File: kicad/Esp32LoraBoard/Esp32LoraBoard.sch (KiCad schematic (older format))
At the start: 13 parts, among them J1 USB_B_Micro, J2 Power-Selector, J3 Testpoints, U1 LM3940IMP-3.3, U2 ESP32-WROOM-32, U3 RFM95W-868S2

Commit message: Diagram approved
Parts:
- added C5, C6: 1n, Capacitor_SMD:C_1206_3216Metric_Pad1.42x1.75mm_HandSolder, symbol Device:C_Small
- added J4: ESP_PROG_JTAG, symbol Connector_Generic:Conn_02x05_Odd_Even
- added J5: Prog, symbol Connector:Conn_01x05_Male
- added Q1: UMH3N, SOT65P230X110-6N, symbol UMH3N:UMH3N
- added R2: 10k, Resistor_SMD:R_1206_3216Metric_Pad1.42x1.75mm_HandSolder, symbol Device:R
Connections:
- net +3V3: now also R2.1
- net GND: now also C5.2, C6.1, J4.3 (Pin_3), J4.5 (Pin_5), J4.7 (Pin_7), J4.9 (Pin_9), J5.1 (Pin_1)
- net TMS: now reaches U2.13 (IO14)
- net TMS: now also J4.2 (Pin_2)
- net TDI: now reaches U2.14 (IO12)
- net TDI: now also J4.8 (Pin_8)
- net TCK: now reaches U2.16 (IO13)
- net TCK: now also J4.4 (Pin_4)
- net TDO: now reaches U2.23 (IO15)
- net TDO: now also J4.6 (Pin_6)
- net Boot: now reaches U2.25 (IO0)
- net Boot: now also C6.2, Q1.3 (C2), R2.2
- net Reset: now reaches R1.2, U2.3 (EN)
- net Reset: now also C5.1, Q1.6 (C1)
- net RX: now reaches U2.34 (RXD0/IO3)
- net RX: now also J5.4 (Pin_4)
- net TX: now reaches U2.35 (TXD0/IO1)
- net TX: now also J5.3 (Pin_3)
- new net DTR: J5.5 (Pin_5), Q1.1 (E1), Q1.5 (B2)
- new net RTS: J5.2 (Pin_2), Q1.2 (B1), Q1.4 (E2)
- no-connect marks 31 -> 26
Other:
- note added: "Boot"
- note added: "GND"
- note added: "RTS"
- note added: "RX"
- note added: "TX"
- moved on the sheet: R1

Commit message: .
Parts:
- removed J3: Testpoints, Connector_PinHeader_2.54mm:PinHeader_1x03_P2.54mm_Vertical, symbol Connector:Conn_01x03_Male
- added J3: Testpoints, symbol Connector:Conn_01x04_Male
- added J6: ext_Measure, symbol Connector:Screw_Terminal_01x04
- added J7: Measurement-Selector, Connector_PinHeader_2.54mm:PinHeader_1x03_P2.54mm_Vertical, symbol Connector:Conn_01x03_Male
- added Q2: Q_NMOS_GSD, symbol Device:Q_NMOS_GSD
- added Q3: SI2301DS, symbol Device:Q_PMOS_GSD
- added R3, R4: 10k, Resistor_SMD:R_1206_3216Metric_Pad1.42x1.75mm_HandSolder, symbol Device:R
- added R5, R6: optional, Resistor_SMD:R_1206_3216Metric_Pad1.42x1.75mm_HandSolder, symbol Device:R
- added R7, R8: 100k, symbol Device:R
- added TP1: TestPoint, symbol Connector:TestPoint
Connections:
- net +3V3: now also C2.1, J2.3 (Pin_3), U1.3 (OUT), J3.4 (Pin_4); no longer C3.1, C4.1, J2.2 (Pin_2), R1.1, R2.1, U2.2 (VDD), U3.13 (3.3V)
- net GND: now also J3.1 (Pin_1), Q2.2 (S), R4.2, R7.2
- net UBAT_ENABLE: now reaches U2.10 (IO25)
- net UBAT_ENABLE: now also Q3.1 (G), R8.2
- net U_EXT_ENABLE: now reaches U2.26 (IO4)
- net U_EXT_ENABLE: now also Q2.1 (G), R7.1
- net UBAT_MEASURE: now reaches U2.6 (IO34)
- net UBAT_MEASURE: now also R3.2, R4.1, TP1.1
- net U_EXT_MEASURE: now reaches U2.7 (IO35)
- net U_EXT_MEASURE: now also J6.2 (Pin_2), R5.2, R6.1
- net V-Batt: now reaches BT1.1 (+), J2.1 (Pin_1)
- net V-Batt: now also J3.2 (Pin_2)
- new net: Q3.2 (S), R3.1
- new net: J6.1 (Pin_1), Q2.3 (D), R6.2
- new net: J6.3 (Pin_3), J7.2 (Pin_2), R5.1
- new net: J6.4 (Pin_4), J7.1 (Pin_1)
- new net VCC: C3.1, C4.1, J2.2 (Pin_2), J3.3 (Pin_3), J7.3 (Pin_3), Q3.3 (D), R1.1, R2.1, R8.1, U2.2 (VDD), U3.13 (3.3V)
- no-connect marks 26 -> 22
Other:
- moved on the sheet: AE1, BT1, C1, C2, C3, C4, C5, C6, J1, J2, R1, R2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

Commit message: schema version 1.0 done
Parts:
- added C7, C8: 100n, Capacitor_SMD:C_1206_3216Metric_Pad1.42x1.75mm_HandSolder, symbol Device:C
- added J8: OLED_128x64, Connector_PinHeader_2.54mm:PinHeader_1x03_P2.54mm_Vertical, symbol Connector:Conn_01x04_Female
- added Q4, Q6: Si2302DS_NMOS, Package_TO_SOT_SMD:TSOT-23_HandSoldering, symbol Device:Q_NMOS_GSD
- added Q5: Si2301DS_PMOS, Package_TO_SOT_SMD:TSOT-23_HandSoldering, symbol Device:Q_PMOS_GSD
- added R10, R11, R13, R9: 10k, Resistor_SMD:R_1206_3216Metric_Pad1.42x1.75mm_HandSolder, symbol Device:R
- added R12: 100k, Resistor_SMD:R_1206_3216Metric_Pad1.42x1.75mm_HandSolder, symbol Device:R
- added TP2: TP_U_EXT, Connector_PinHeader_2.54mm:PinHeader_1x01_P2.54mm_Vertical, symbol Connector:TestPoint
- added TP3: VCC_2, Connector_PinHeader_2.54mm:PinHeader_1x01_P2.54mm_Vertical, symbol Connector:TestPoint
- J3: footprint (none) -> Connector_PinHeader_2.54mm:PinHeader_1x04_P2.54mm_Vertical
- J4: footprint (none) -> Connector_PinHeader_1.27mm:PinHeader_2x05_P1.27mm_Vertical
- J5: footprint (none) -> Connector_PinHeader_2.54mm:PinHeader_1x05_P2.54mm_Vertical
- J6: footprint (none) -> Connector_Phoenix_MSTB:PhoenixContact_MSTBVA_2,5_4-G-5,08_1x04_P5.08mm_Vertical
- Q1: footprint SOT65P230X110-6N -> lib_fp:SOT65P230X110-6N
- Q2: value Q_NMOS_GSD -> Si2302DS_NMOS; footprint (none) -> Package_TO_SOT_SMD:TSOT-23_HandSoldering
- Q3: value SI2301DS -> Si2301DS_PMOS; footprint (none) -> Package_TO_SOT_SMD:TSOT-23_HandSoldering
- R7, R8: footprint (none) -> Resistor_SMD:R_1206_3216Metric_Pad1.42x1.75mm_HandSolder
- TP1: value TestPoint -> TP_U_BATT; footprint (none) -> Connector_PinHeader_2.54mm:PinHeader_1x01_P2.54mm_Vertical
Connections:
- net GND: now also C7.1, C8.2, J8.1 (Pin_1)
- net U_EXT_ENABLE: now also TP2.1
- net VCC: now also C7.2, Q5.3 (D), R10.1, R12.1, R13.1
- net POWER_ENABLE: now reaches U2.27 (IO16)
- net POWER_ENABLE: now also Q5.1 (G), R12.2
- net SDA: now reaches U2.33 (IO21)
- net SDA: now also Q4.3 (D), R10.2
- net SCL: now reaches U2.36 (IO22)
- net SCL: now also Q6.3 (D), R13.2
- new net SCL_2: J8.3 (Pin_3), Q6.2 (S), R11.2
- new net SDA_2: J8.4 (Pin_4), Q4.2 (S), R9.2
- new net VCC_2: C8.1, J8.2 (Pin_2), Q4.1 (G), Q5.2 (S), Q6.1 (G), R11.1, R9.1, TP3.1
- no-connect marks 22 -> 19
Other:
- note added: "Lora Pins"
- note added: "OLED Display via Levelshifter connected to I2C bus"
- note added: "Pripherie can be switched off"
- note added: "Voltage Measurement (internal and external)"
- moved on the sheet: J4, J6, J7, Q2, Q3, R3, R4, R5, R6, R7, R8, TP1

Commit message: .
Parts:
- BT1: footprint Connector_Phoenix_MSTB:PhoenixContact_MSTBA_2,5_2-G-5,08_1x02_P5.08mm_Horizontal -> Connector_Phoenix_MSTB:PhoenixContact_MSTBVA_2,5_2-G-5,08_1x02_P5.08mm_Vertical
- J3: footprint Connector_PinHeader_2.54mm:PinHeader_1x04_P2.54mm_Vertical -> Connector_PinHeader_2.54mm:PinHeader_1x05_P2.54mm_Vertical; symbol Connector:Conn_01x04_Male -> Connector:Conn_01x05_Male
- J8: footprint Connector_PinHeader_2.54mm:PinHeader_1x03_P2.54mm_Vertical -> Connector_PinHeader_2.54mm:PinHeader_1x04_P2.54mm_Vertical
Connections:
- net +3V3: now also J3.3 (Pin_3); no longer J3.4 (Pin_4)
- net VCC: now also J3.4 (Pin_4); no longer J3.3 (Pin_3)
- net VCC_2: now also J3.5 (Pin_5)
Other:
- note added: "Optional Power Supply"
- moved on the sheet: C8, J4, J5, Q1, Q5, R12, TP3

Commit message: .
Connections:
- net ext.Voltage: now reaches J6.4 (Pin_4), J7.1 (Pin_1)
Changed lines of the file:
@@
 encoding utf-8
 Sheet 1 1
-Title "EspLoraBoard"
+Title "Esp32LoraBoard"
 Date "2020-03-22"
 Rev "1.0"
@@
 P 1600 4900
 F 0 "J6" H 1650 4450 50  0000 C CNN
-F 1 "ext_Measure" H 1650 4550 50  0000 C CNN
+F 1 "ext_Measure" H 1750 4550 50  0000 C CNN
 F 2 "Connector_Phoenix_MSTB:PhoenixContact_MSTBVA_2,5_4-G-5,08_1x04_P5.08mm_Vertical" H 1600 4900 50  0001 C CNN
 F 3 "~" H 1600 4900 50  0001 C CNN
@@
 Text Notes 1100 1800 0    50   ~ 0
 Optional Power Supply
+Text Label 1800 4600 1    50   ~ 0
+ext.Voltage
 $EndSCHEMATC

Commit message: .
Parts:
- added C10, C9: 1u, Capacitor_SMD:C_1206_3216Metric_Pad1.42x1.75mm_HandSolder, symbol Device:C
- added R14, R15: 10k, Resistor_SMD:R_1206_3216Metric_Pad1.42x1.75mm_HandSolder, symbol Device:R
- added SW1: Rotary_Encoder, Rotary_Encoder:RotaryEncoder_Alps_EC11E-Switch_Vertical_H20mm, symbol Device:Rotary_Encoder_Switch
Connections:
- net GND: now also C10.2, C9.2, SW1.C, SW1.S2
- net VCC_2: now also R14.1, R15.1
- net ROT_SW: now reaches U2.28 (IO17)
- net ROT_SW: now also SW1.S1
- net ROT_A: now reaches U2.4 (SENSOR_VP)
- net ROT_A: now also C9.1, R14.2, SW1.A
- net ROT_B: now reaches U2.5 (SENSOR_VN)
- net ROT_B: now also C10.1, R15.2, SW1.B
- no-connect marks 19 -> 16
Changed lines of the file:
@@
 	6650 2200 6650 2250
 NoConn ~ 7700 2850
-NoConn ~ 7700 3750
 NoConn ~ 6500 3850
-NoConn ~ 6500 2850
-NoConn ~ 6500 2950
 NoConn ~ 6500 3950
 NoConn ~ 6500 4050
@@
 Text Label 1800 4600 1    50   ~ 0
 ext.Voltage
+$Comp
+L Device:Rotary_Encoder_Switch SW1
+U 1 1 5E862008
+P 7000 7700
+F 0 "SW1" H 7000 7400 50  0000 C CNN
+F 1 "Rotary_Encoder" H 7000 8000 50  0000 C CNN
+F 2 "Rotary_Encoder:RotaryEncoder_Alps_EC11E-Switch_Vertical_H20mm" H 6850 7860 50  0001 C CNN
+F 3 "~" H 7000 7960 50  0001 C CNN
+	1    7000 7700
+	1    0    0    -1
+$EndComp
+$Comp
+L Device:R R14
+U 1 1 5E865359
+P 6050 7300
+F 0 "R14" H 6120 7346 50  0000 L CNN
+F 1 "10k" H 6120 7255 50  0000 L CNN
+F 2 "Resistor_SMD:R_1206_3216Metric_Pad1.42x1.75mm_HandSolder" V 5980 7300 50  0001 C CNN
+F 3 "~" H 6050 7300 50  0001 C CNN
+	1    6050 7300
+	1    0    0    -1
+$EndComp
+$Comp
+L Device:R R15
+U 1 1 5E86599D
+P 6300 7300
+F 0 "R15" H 6370 7346 50  0000 L CNN
+F 1 "10k" H 6370 7255 50  0000 L CNN
+F 2 "Resistor_SMD:R_1206_3216Metric_Pad1.42x1.75mm_HandSolder" V 6230 7300 50  0001 C CNN
+F 3 "~" H 6300 7300 50  0001 C CNN
+	1    6300 7300
+	1    0    0    -1
+$EndComp
+$Comp
+L Device:C C9
+U 1 1 5E865D88
+P 6050 8000
+F 0 "C9" H 5800 8050 50  0000 L CNN
+F 1 "1u" H 5800 7950 50  0000 L CNN
+F 2 "Capacitor_SMD:C_1206_3216Metric_Pad1.42x1.75mm_HandSolder" H 6088 7850 50  0001 C CNN
+F 3 "~" H 6050 8000 50  0001 C CNN
+	1    6050 8000
+	1    0    0    -1
+$EndComp
+$Comp
+L Device:C C10
+U 1 1 5E86621D
+P 6300 8000
+F 0 "C10" H 6415 8046 50  0000 L CNN
+F 1 "1u" H 6415 7955 50  0000 L CNN
+F 2 "Capacitor_SMD:C_1206_3216Metric_Pad1.42x1.75mm_HandSolder" H 6338 7850 50  0001 C CNN
+F 3 "~" H 6300 8000 50  0001 C CNN
+	1    6300 8000
+	1    0    0    -1
+$EndComp
+Wire Wire Line
+	6050 7100 6300 7100
+Wire Wire Line
+	6300 7100 6300 7150
+Connection ~ 6050 7100
+Wire Wire Line
+	6050 7100 6050 7150
+Wire Wire Line
+	6050 7450 6050 7600
+Wire Wire Line
+	6300 7450 6300 7800
+Wire Wire Line
+	6050 8150 6050 8250
+Wire Wire Line
+	6050 8250 6300 8250
+Wire Wire Line
+	7400 8250 7400 7800
+Wire Wire Line
+	7400 7800 7300 7800
+Wire Wire Line
+	6300 8150 6300 8250
+Connection ~ 6300 8250
+Connection ~ 6300 7800
+Wire Wire Line
+	6300 7800 6300 7850
+Wire Wire Line
+	6700 7600 6550 7600
+Connection ~ 6050 7600
+Wire Wire Line
+	6050 7600 6050 7850
+Wire Wire Line
+	6050 6900 6050 7100
+Text Label 6050 6900 1    50   ~ 0
+VCC_2
+Wire Wire Line
+	6550 7600 6550 6900
+Wire Wire Line
+	6300 8250 6550 8250
+Wire Wire Line
+	6300 7800 6650 7800
+Wire Wire Line
+	6050 7600 6550 7600
+Connection ~ 6550 7600
+Wire Wire Line
+	6650 7800 6650 6900
+Connection ~ 6650 7800
+Wire Wire Line
+	6650 7800 6700 7800
+Wire Wire Line
+	6700 7700 6550 7700
+Wire Wire Line
+	6550 7700 6550 8250
+Connection ~ 6550 8250
+Wire Wire Line
+	6550 8250 7400 8250
+Wire Wire Line
+	7300 7600 7300 6900
+Text Label 6550 6900 1    50   ~ 0
+ROT_A
+Text Label 6650 6900 1    50   ~ 0
+ROT_B
+Text Label 7300 6900 1    50   ~ 0
+ROT_SW
+Wire Notes Line
+	7750 6400 7750 8500
+Wire Notes Line
+	7750 8500 5650 8500
+Wire Notes Line
+	5650 8500 5650 6400
+Wire Notes Line
+	5650 6400 7750 6400
+Wire Wire Line
+	7700 3750 8000 3750
+Wire Wire Line
+	6500 2950 6200 2950
+Wire Wire Line
+	6500 2850 6200 2850
+Text Label 6200 2850 0    50   ~ 0
+ROT_A
+Text Label 6200 2950 0    50   ~ 0
+ROT_B
+Text Label 8000 3750 2    50   ~ 0
+ROT_SW
+$Comp
+L power:GND #PWR014
+U 1 1 5E9DC8F4
+P 6550 8300
+F 0 "#PWR014" H 6550 8050 50  0001 C CNN
+F 1 "GND" H 6400 8300 50  0000 C CNN
+F 2 "" H 6550 8300 50  0001 C CNN
+F 3 "" H 6550 8300 50  0001 C CNN
+	1    6550 8300
+	1    0    0    -1
+$EndComp
+Wire Wire Line
+	6550 8300 6550 8250
 $EndSCHEMATC

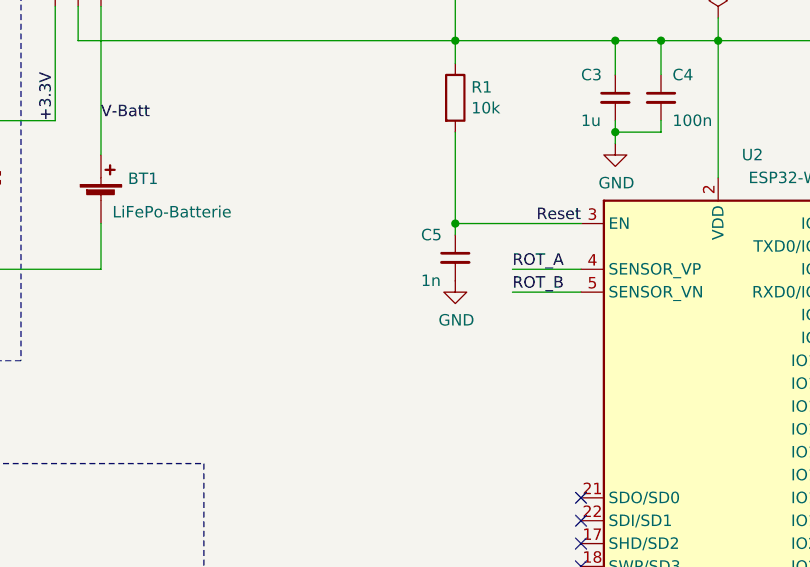
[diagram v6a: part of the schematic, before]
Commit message: Reset Button added
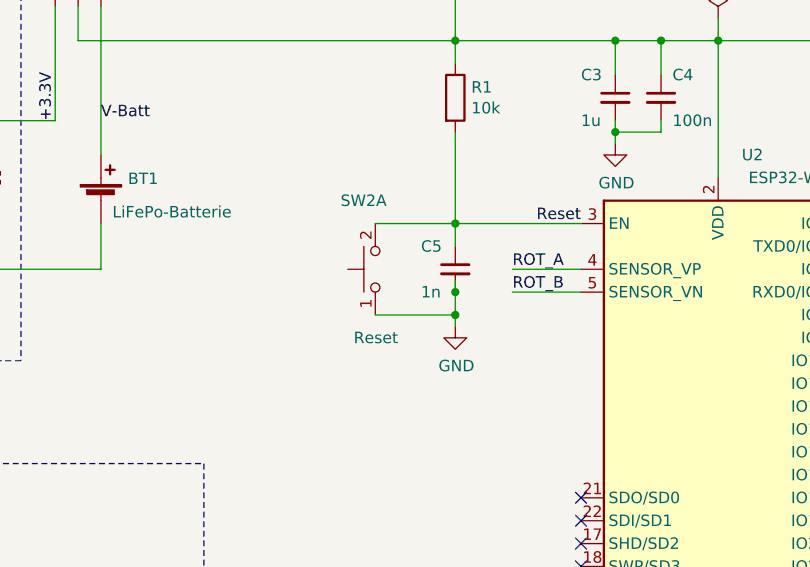
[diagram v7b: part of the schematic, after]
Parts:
- added SW2: Reset, Button_Switch_SMD:SW_SPST_CK_RS282G05A3, symbol Switch:SW_Push_Dual_x2
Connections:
- net GND: now also SW2.1 (C)
- net Reset: now also SW2.2 (D)
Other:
- moved on the sheet: C5
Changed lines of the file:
@@
 Sheet 1 1
 Title "Esp32LoraBoard"
-Date "2020-03-22"
-Rev "1.0"
+Date "2020-04-11"
+Rev "1.1"
 Comp "Viktor Rees"
-Comment1 ""
+Comment1 "Reset-Button added"
 Comment2 ""
 Comment3 ""
@@
 L Device:C_Small C5
 U 1 1 5E7C919D
-P 5950 2800
-F 0 "C5" H 5800 2900 50  0000 L CNN
-F 1 "1n" H 5800 2700 50  0000 L CNN
-F 2 "Capacitor_SMD:C_1206_3216Metric_Pad1.42x1.75mm_HandSolder" H 5950 2800 50  0001 C CNN
-F 3 "~" H 5950 2800 50  0001 C CNN
-	1    5950 2800
+P 5950 2850
+F 0 "C5" H 5800 2950 50  0000 L CNN
+F 1 "1n" H 5800 2750 50  0000 L CNN
+F 2 "Capacitor_SMD:C_1206_3216Metric_Pad1.42x1.75mm_HandSolder" H 5950 2850 50  0001 C CNN
+F 3 "~" H 5950 2850 50  0001 C CNN
+	1    5950 2850
 	1    0    0    -1
 $EndComp
@@
 L power:GND #PWR0102
 U 1 1 5E7E119F
-P 5950 2900
-F 0 "#PWR0102" H 5950 2650 50  0001 C CNN
-F 1 "GND" H 5955 2727 50  0000 C CNN
-F 2 "" H 5950 2900 50  0001 C CNN
-F 3 "" H 5950 2900 50  0001 C CNN
-	1    5950 2900
-	1    0    0    -1
-$EndComp
-Wire Wire Line
-	5950 2700 5950 2650
-Connection ~ 5950 2650
+P 5950 3100
+F 0 "#PWR0102" H 5950 2850 50  0001 C CNN
+F 1 "GND" H 5955 2927 50  0000 C CNN
+F 2 "" H 5950 3100 50  0001 C CNN
+F 3 "" H 5950 3100 50  0001 C CNN
+	1    5950 3100
+	1    0    0    -1
+$EndComp
 Text Label 14100 1200 0    50   ~ 0
 Reset
@@
 Wire Wire Line
 	6550 8300 6550 8250
+$Comp
+L Switch:SW_Push_Dual_x2 SW2
+U 1 1 5E94C2C5
+P 5600 2850
+F 0 "SW2" V 5900 2800 50  0000 L CNN
+F 1 "Reset" V 5300 2750 50  0000 L CNN
+F 2 "Button_Switch_SMD:SW_SPST_CK_RS282G05A3" H 5600 3050 50  0001 C CNN
+F 3 "~" H 5600 3050 50  0001 C CNN
+	1    5600 2850
+	0    -1   -1   0
+$EndComp
+Wire Wire Line
+	5950 2900 5950 2950
+Wire Wire Line
+	5600 3050 5950 3050
+Connection ~ 5950 2950
+Wire Wire Line
+	5950 2950 5950 3050
+Wire Wire Line
+	5600 2650 5950 2650
+Connection ~ 5950 2650
+Wire Wire Line
+	5950 2650 5950 2750
+Wire Wire Line
+	5950 3100 5950 3050
+Connection ~ 5950 3050
 $EndSCHEMATC

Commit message: Kicad Version V1.1
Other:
- note added: "DTR"
- note removed: "Boot"
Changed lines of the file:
@@
 RX
 Text Notes 12100 1450 2    50   ~ 0
-Boot
+DTR
 Text Notes 12100 1150 2    50   ~ 0
 RTS
@@
 Wire Wire Line
 	14650 6250 14900 6250
-Wire Wire Line
-	14650 5700 14650 5850
-$Comp
-L power:VCC #PWR013
-U 1 1 5E9A78A9
-P 14650 5700
-F 0 "#PWR013" H 14650 5550 50  0001 C CNN
-F 1 "VCC" H 14667 5873 50  0000 C CNN
-F 2 "" H 14650 5700 50  0001 C CNN
-F 3 "" H 14650 5700 50  0001 C CNN
-	1    14650 5700
-	1    0    0    -1
-$EndComp
 Text Label 14150 5700 1    50   ~ 0
 VCC_2
@@
 Wire Wire Line
 	13300 6250 13550 6250
-Wire Wire Line
-	13300 5700 13300 5850
-$Comp
-L power:VCC #PWR010
-U 1 1 5E93EE29
-P 13300 5700
-F 0 "#PWR010" H 13300 5550 50  0001 C CNN
-F 1 "VCC" H 13317 5873 50  0000 C CNN
-F 2 "" H 13300 5700 50  0001 C CNN
-F 3 "" H 13300 5700 50  0001 C CNN
-	1    13300 5700
-	1    0    0    -1
-$EndComp
 Text Label 12800 5700 1    50   ~ 0
 VCC_2
@@
 Wire Wire Line
 	13050 5950 13050 5800
-Wire Wire Line
-	13050 5800 12800 5800
 Connection ~ 12800 5800
 Wire Wire Line
@@
 	5950 3100 5950 3050
 Connection ~ 5950 3050
+Wire Wire Line
+	13050 5800 12800 5800
+Wire Wire Line
+	14650 5700 14650 5850
+$Comp
+L power:VCC #PWR013
+U 1 1 5E9A78A9
+P 14650 5700
+F 0 "#PWR013" H 14650 5550 50  0001 C CNN
+F 1 "VCC" H 14667 5873 50  0000 C CNN
+F 2 "" H 14650 5700 50  0001 C CNN
+F 3 "" H 14650 5700 50  0001 C CNN
+	1    14650 5700
+	1    0    0    -1
+$EndComp
+Wire Wire Line
+	13300 5700 13300 5850
+$Comp
+L power:VCC #PWR010
+U 1 1 5E93EE29
+P 13300 5700
+F 0 "#PWR010" H 13300 5550 50  0001 C CNN
+F 1 "VCC" H 13317 5873 50  0000 C CNN
+F 2 "" H 13300 5700 50  0001 C CNN
+F 3 "" H 13300 5700 50  0001 C CNN
+	1    13300 5700
+	1    0    0    -1
+$EndComp
 $EndSCHEMATC
